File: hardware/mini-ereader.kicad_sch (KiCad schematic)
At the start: 0 parts

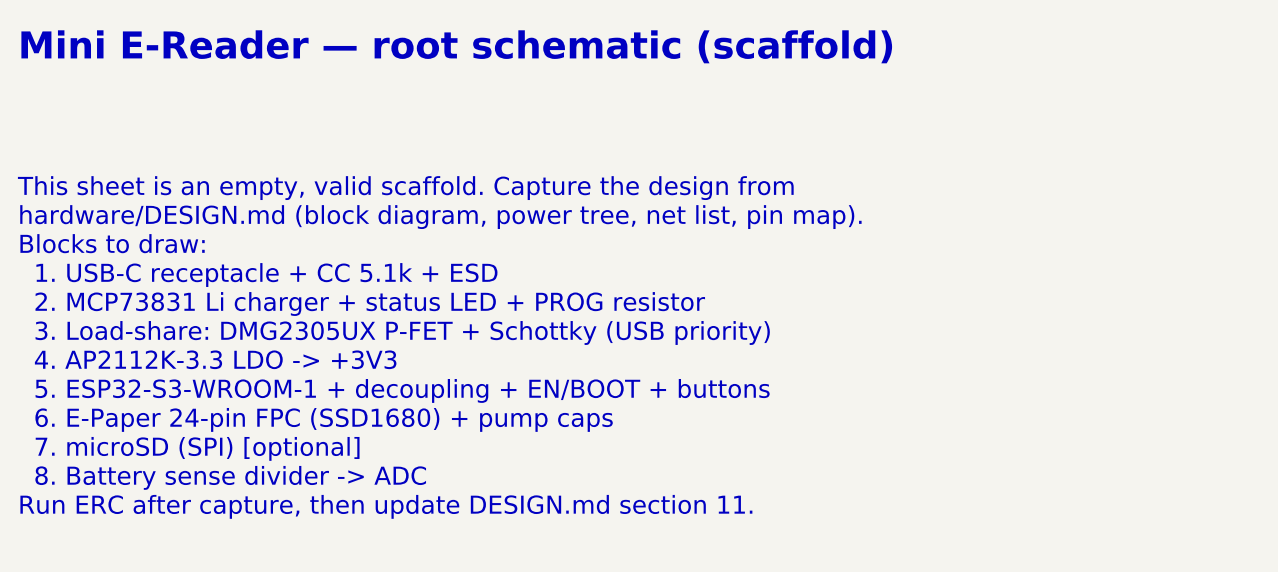
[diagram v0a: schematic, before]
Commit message: Adapt repo to Mini E-Reader; add 4.26" display + frontlight + KiCad CI
Full Colophon->project adaptation and incorporation of the owner-supplied
Good Display FL0426-S01C frontlight datasheet.

Project docs (Colophon "adopt forward"):
- README.md rewritten as the Mini E-Reader Brief.
- docs/adr/0001-0005 = e-reader decisions (MCU, display+frontlight, power,
  native-USB programming, frontlight driver).
- docs/research-log.md, docs/runbook.md, CHANGELOG.md restarted for the
  project.

Display/frontlight (from FL0426-S01C):
- Corrected display to 4.26" 800x480 EPD (was a 2.13" assumption). The PDF
  is a FRONTLIGHT module, not the panel: tunable white, 2 channels of 5
  series LEDs (VF<=15V, IF<=15mA), 6-pin FPC (1 LEDC+ 2 LEDC- 3/4 NC
  5 LEDW+ 6 LEDW-).
- Added frontlight subsystem: connector J5 + 2x TPS61165 constant-current
  boost drivers, PWM-dimmed from GPIO15/16 (cold/warm). ADR 0005.
- DESIGN.md, BOM.csv, gen_netlist_skidl.py, and the KiCad scaffold updated
  (board outline ~66x115mm; sch/pcb notes).

KiCad-capable environment:
- .github/workflows/kicad.yml runs kicad-cli (kicad/kicad:8.0) ERC/DRC and
  exports a schematic PDF + gerbers as artifacts on push.

Still needed: the EPD panel's own datasheet to lock the display FPC pinout
and controller (DESIGN.md section 5, BOM J4).

Note: file deletion was blocked by the sandbox, so Colophon leftovers
remain and are pending removal: docs/adr/{0001-minimal-by-default,
0002-markdown-in-git,0003-just-in-time-over-upfront,0004-naming-conventions,
0005-coverage-mapping}.md, docs/faq.md, docs/adoption.md, and hardware/docs/
(now pointer stubs). docs/adr/ therefore has temporary duplicate numbering.

Validated: JSON parses, Python compiles, KiCad S-expressions balanced,
workflow YAML parses.

Co-Authored-By: Claude Opus 4.8 <noreply@anthropic.com>
Claude-Session: https://claude.ai/code/session_01XLMfdr5mHwD9XVwrMpqCsJ
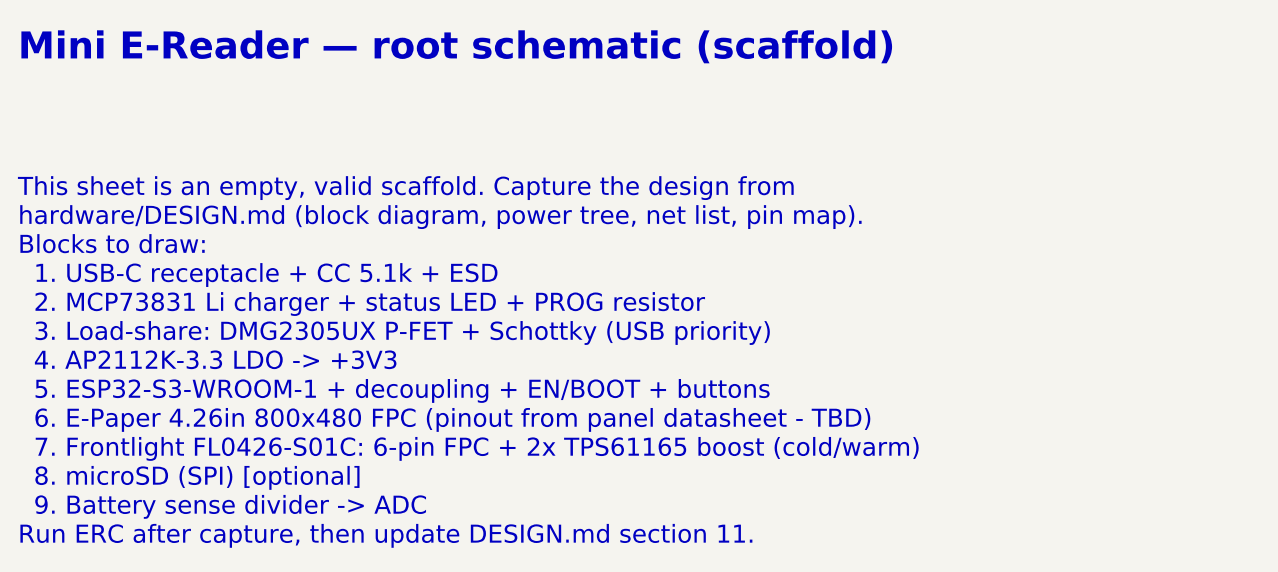
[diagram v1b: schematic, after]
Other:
- note added: "This sheet is an empty, valid scaffold. Capture the design from hardware/DESIGN.md (block diagram, power tree, net list, pin map). Blocks to draw: 1. USB-C receptacle + CC 5.1k + ESD 2. MCP73831 Li charger + status LED + PROG resistor 3. Load-share: DMG2305UX P-FET + Schottky (USB priority) 4. AP2112K-3.3 LDO -> +3V3 5. ESP32-S3-WROOM-1 + decoupling + EN/BOOT + buttons 6. E-Paper 4.26in 800x480 F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"
- note removed: "This sheet is an empty, valid scaffold. Capture the design from hardware/DESIGN.md (block diagram, power tree, net list, pin map). Blocks to draw: 1. USB-C receptacle + CC 5.1k + ESD 2. MCP73831 Li charger + status LED + PROG resistor 3. Load-share: DMG2305UX P-FET + Schottky (USB priority) 4. AP2112K-3.3 LDO -> +3V3 5. ESP32-S3-WROOM-1 + decoupling + EN/BOOT + buttons 6. E-Paper 24-pin FPC (SSD1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"
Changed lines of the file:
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@@
 		(rev "0.1")
 		(company "Craft Code Systems")
-		(comment 1 "ESP32-S3 + SPI E-Paper (SSD1680) reference design")
+		(comment 1 "ESP32-S3 + 4.26in 800x480 E-Paper + tunable frontlight")
 		(comment 2 "Capture this schematic from hardware/DESIGN.md")
 	)
@@
 		)
 	)
-	(text "This sheet is an empty, valid scaffold. Capture the design from\nhardware/DESIGN.md (block diagram, power tree, net list, pin map).\nBlocks to draw:\n  1. USB-C receptacle + CC 5.1k + ESD\n  2. MCP73831 Li charger + status LED + PROG resistor\n  3. Load-share: DMG2305UX P-FET + Schottky (USB priority)\n  4. AP2112K-3.3 LDO -> +3V3\n  5. ESP32-S3-WROOM-1 + decoupling + EN/BOOT + buttons\n  6. E-Paper 24-pin FPC (SSD1680) + pump caps\n  7. microSD (SPI) [optional]\n  8. Battery sense divider -> ADC\nRun ERC after capture, then update DESIGN.md section 11."
+	(text "This sheet is an empty, valid scaffold. Capture the design from\nhardware/DESIGN.md (block diagram, power tree, net list, pin map).\nBlocks to draw:\n  1. USB-C receptacle + CC 5.1k + ESD\n  2. MCP73831 Li charger + status LED + PROG resistor\n  3. Load-share: DMG2305UX P-FET + Schottky (USB priority)\n  4. AP2112K-3.3 LDO -> +3V3\n  5. ESP32-S3-WROOM-1 + decoupling + EN/BOOT + buttons\n  6. E-Paper 4.26in 800x480 FPC (pinout from panel datasheet - TBD)\n  7. Frontlight FL0426-S01C: 6-pin FPC + 2x TPS61165 boost (cold/warm)\n  8. microSD (SPI) [optional]\n  9. Battery sense divider -> ADC\nRun ERC after capture, then update DESIGN.md section 11."
 		(exclude_from_sim no)
 		(at 25.4 38.1 0)
